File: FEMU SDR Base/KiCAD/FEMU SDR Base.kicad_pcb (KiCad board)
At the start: 4 copper layers, 164.8 x 164.8 mm, 33 parts, among them P2 SDR_Shield_1, P3 SDR_Shield_2, P8 Raspi_Power_Shield, U1 TPS562209, U2 SDR_1_LDO_1_2V, U3 SDR_2_LDO_1_2V, U4 SDR_1_LDO_3_3V, U5 SDR_2_LDO_3_3V

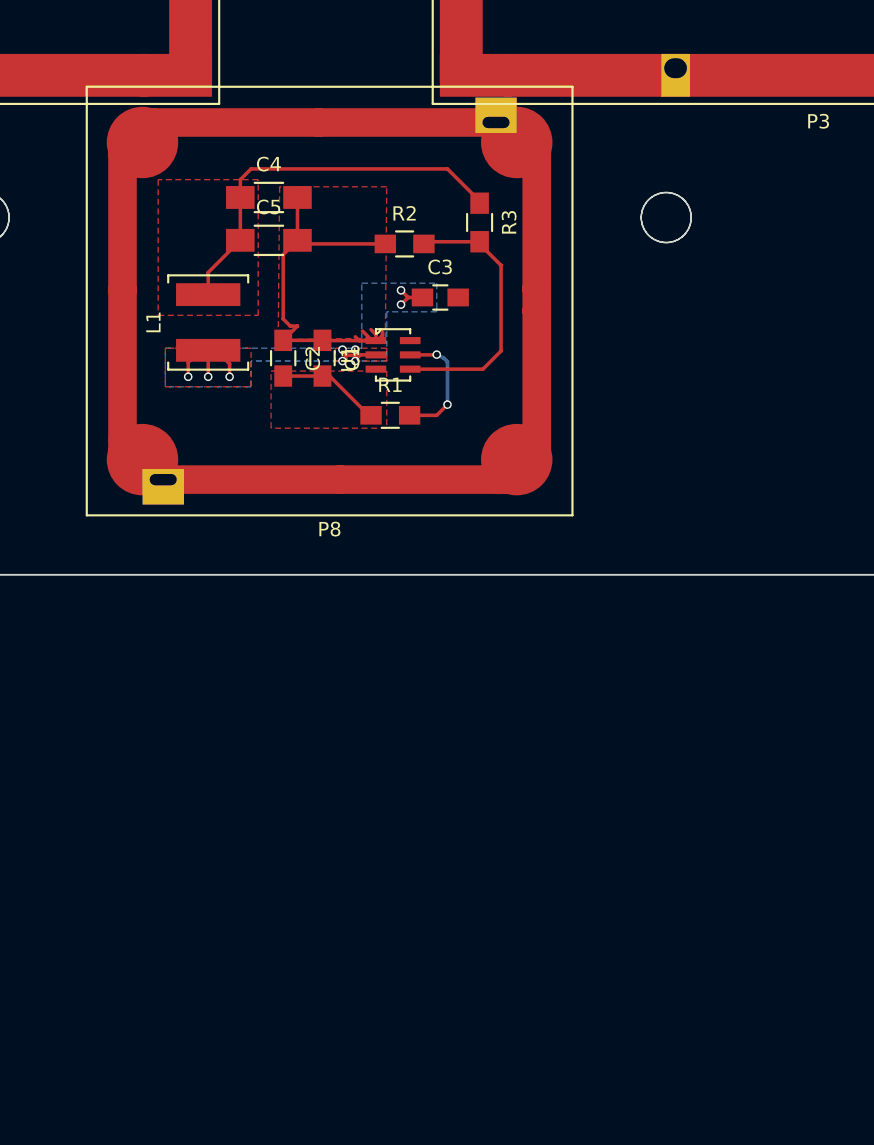
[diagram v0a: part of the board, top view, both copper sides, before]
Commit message: Added keepout zones for mechanical structures
Signed-off-by: hardiepienaar <hardiepienaar@gmail.com>
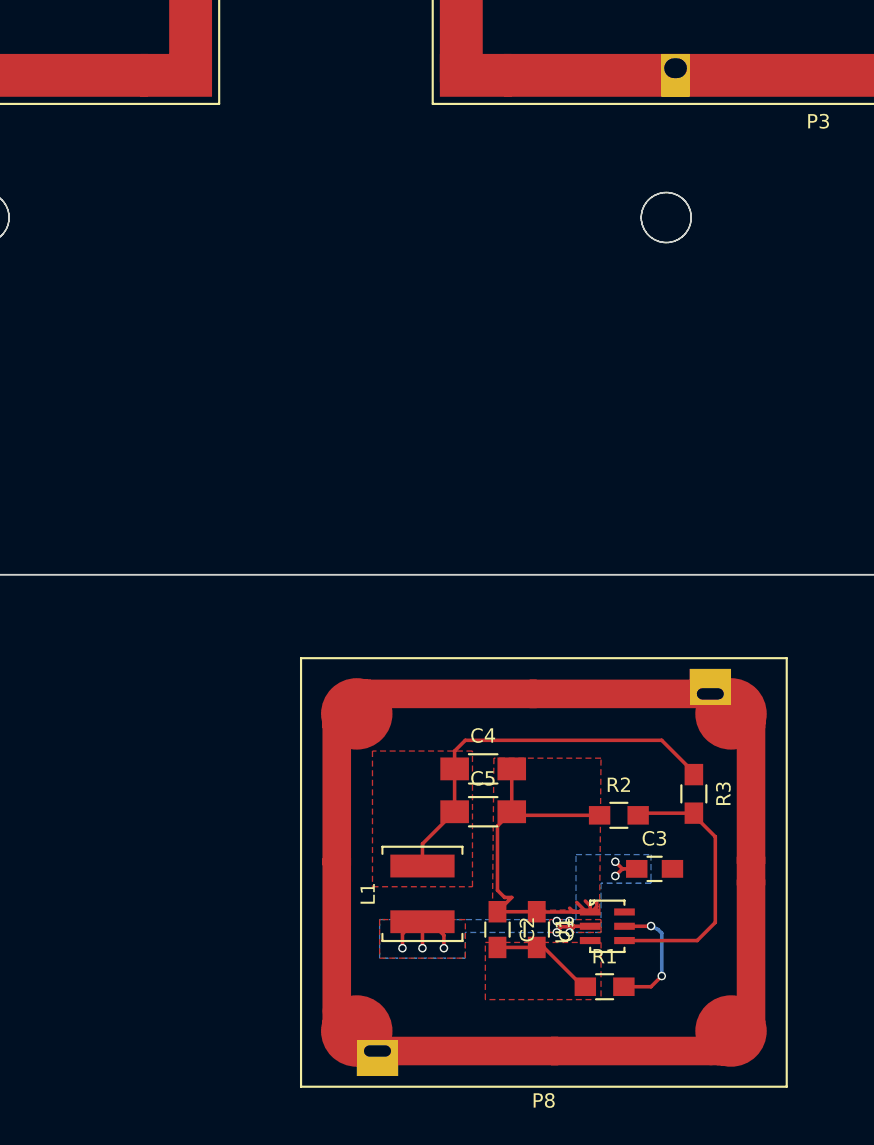
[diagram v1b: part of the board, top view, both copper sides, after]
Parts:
- moved C1 42.7 mm to (99.3, 181.9)
- moved C2 42.7 mm to (96.6, 181.9)
- moved C3 42.7 mm to (107.6, 177.7)
- moved C4 42.7 mm to (95.6, 170.7)
- moved C5 42.7 mm to (95.6, 173.7)
- moved L1 42.7 mm to (91.3, 179.4)
- moved P8 42.7 mm to (99.8, 177.9)
- moved R1 42.7 mm to (104.1, 185.9)
- moved R2 42.7 mm to (105.1, 173.9)
- moved R3 42.7 mm to (110.3, 172.4)
- moved U1 42.7 mm to (104.3, 181.7)
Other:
- board text added: "Cable tray area"
- board text added: "Power"

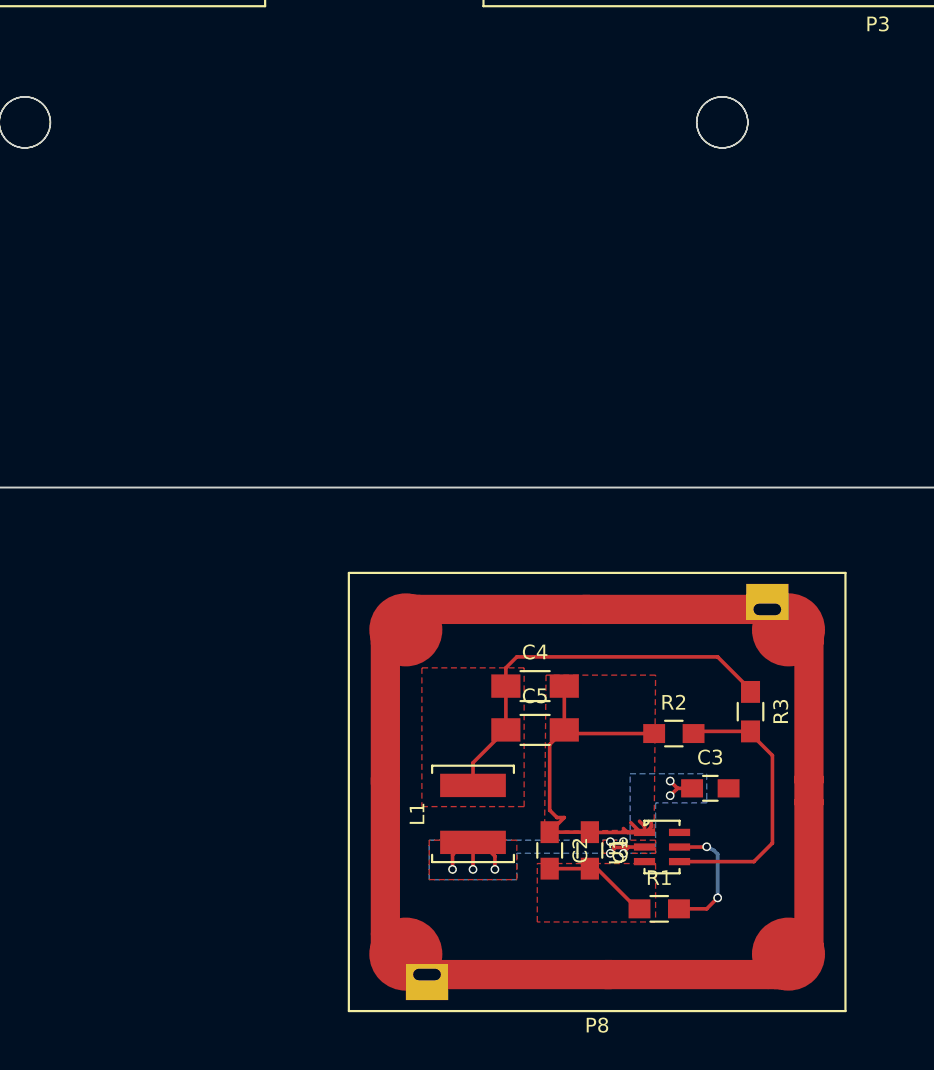
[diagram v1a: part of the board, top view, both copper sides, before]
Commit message: STATUS = FREE, RASPI PSU smaller layout, footprints swapped
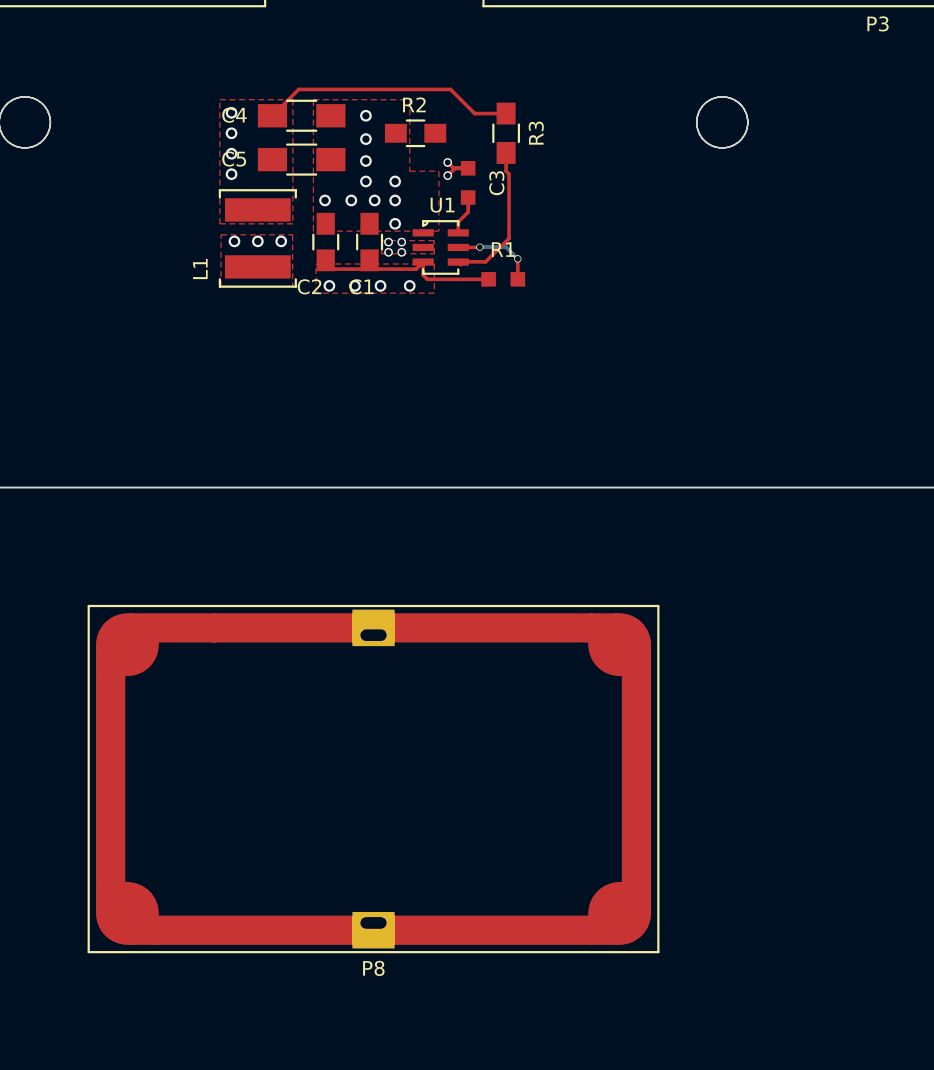
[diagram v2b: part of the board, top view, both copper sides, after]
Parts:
- P8: footprint ARB_foots:PCB_Shield_29x25mm -> ARB_foots:PCB_Shield_35x20mm
- moved R2 44.7 mm to (87.4, 132.8)
- moved C3 44.6 mm to (91.0, 136.2), turned to 270 degrees
- moved R1 44.4 mm to (93.4, 142.8)
- moved C2 44.4 mm to (81.2, 140.2)
- moved C1 44.3 mm to (84.2, 140.2)
- moved U1 43.8 mm to (89.1, 140.6)
- moved R3 43.0 mm to (93.6, 132.8)
- moved C4 42.2 mm to (79.6, 131.6)
- moved C5 42.2 mm to (79.6, 134.6)
- moved L1 42.1 mm to (76.6, 140.0)
- moved P8 15.3 mm to (84.5, 177.0)
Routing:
- net Earth: track 28.9 -> 0.39 mm
- net /VSW: track 14.4 -> 3.17 mm, vias 9 -> 2
- net GND: track 10.7 -> 0.00 mm
- net +5V: track 27.1 -> 17.4 mm
- net Net-(R2-Pad2): track 19.1 -> 10.3 mm
- net +12V: track 7.29 -> 12.7 mm
- net Net-(R1-Pad2): track 8.73 -> 5.82 mm
- net Net-(C3-Pad2): track 0.00 -> 2.70 mm
- net (no net): vias 0 -> 25
- added copper zone on 12V, net /VSW
- removed copper zone on B.Cu, net /VSW
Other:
- net class Default: via_dia 0.6 -> 0.5
- rule trace_min: 0.2 -> 0.155
- rule via_min_drill: 0.3 -> 0.33
- rule via_min_size: 0.4 -> 0.18

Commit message: Added pads for power, usb and pwm distribution
Signed-off-by: hardiepienaar <hardiepienaar@gmail.com>
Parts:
- added P10: PWM2, SMD_Packages:SMD-1206_Pol, F.Cu at (77.5, 28.2)
- added P11: PWM3, SMD_Packages:SMD-1206_Pol, F.Cu at (82.2, 28.2)
- added P12: PWM4, SMD_Packages:SMD-1206_Pol, F.Cu at (87.0, 28.2)
- added P13: PWM1, SMD_Packages:SMD-1206_Pol, F.Cu at (29.5, 127.8)
- added P14: PWM2, SMD_Packages:SMD-1206_Pol, F.Cu at (24.5, 41.8)
- added P15: PWM3, SMD_Packages:SMD-1206_Pol, F.Cu at (28.5, 41.8)
- added P16: PWM4, SMD_Packages:SMD-1206_Pol, F.Cu at (144.5, 41.8)
- added P17: 12V, SMD_Packages:1Pin, F.Cu at (128.5, 41.8)
- added P18: GND, SMD_Packages:1Pin, F.Cu at (134.5, 41.8)
- added P19: 12V, SMD_Packages:1Pin, F.Cu at (128.5, 127.8)
- added P20: GND, SMD_Packages:1Pin, F.Cu at (134.5, 127.8)
- added P21: S0GND, SMD_Packages:1Pin, F.Cu at (46.5, 177.8)
- added P22: S1GND, SMD_Packages:1Pin, F.Cu at (40.5, 177.8)
- added P23: S0DN, SMD_Packages:1Pin, F.Cu at (37.5, 186.2)
- added P24: S1DN, SMD_Packages:1Pin, F.Cu at (35.0, 185.8)
- added P25: S0DP, SMD_Packages:1Pin, F.Cu at (36.0, 186.8)
- added P26: S1DP, SMD_Packages:1Pin, F.Cu at (27.5, 185.8)
- added P27: PWM0, SMD_Packages:SMD-1206_Pol, F.Cu at (68.0, 28.2)
- added P28: PWM5, SMD_Packages:SMD-1206_Pol, F.Cu at (91.8, 28.2)
- added P29: PWM6, SMD_Packages:SMD-1206_Pol, F.Cu at (96.5, 28.2)
- added P30: PWM7, SMD_Packages:SMD-1206_Pol, F.Cu at (101.2, 28.2)
- added P31: PWM0, SMD_Packages:SMD-1206_Pol, F.Cu at (24.5, 127.8)
- added P32: PWM5, SMD_Packages:SMD-1206_Pol, F.Cu at (140.5, 41.8)
- added P33: PWM6, SMD_Packages:SMD-1206_Pol, F.Cu at (144.5, 127.8)
- added P34: PWM7, SMD_Packages:SMD-1206_Pol, F.Cu at (140.5, 127.8)
- added P4: 12V, SMD_Packages:1Pin, F.Cu at (40.5, 41.8)
- added P5: GND, SMD_Packages:1Pin, F.Cu at (36.0, 127.8)
- added P6: 12V, SMD_Packages:1Pin, F.Cu at (41.5, 127.8)
- added P7: GND, SMD_Packages:1Pin, F.Cu at (34.5, 41.8)
- added P9: PWM1, SMD_Packages:SMD-1206_Pol, F.Cu at (72.8, 28.2)
- moved P8 42.0 mm to (84.5, 135.0)
- moved C1 2.00 mm to (84.2, 138.2)
- moved C2 2.00 mm to (81.2, 138.2)
- moved C3 2.00 mm to (91.0, 134.2)
- moved C4 2.00 mm to (79.6, 129.6)
- moved C5 2.00 mm to (79.6, 132.6)
- moved L1 2.00 mm to (76.6, 138.0)
- moved R1 2.00 mm to (93.4, 140.8)
- moved R2 2.00 mm to (87.4, 130.8)
- moved R3 2.00 mm to (93.6, 130.8)
- moved U1 2.00 mm to (89.1, 138.6)
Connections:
- C1 pad 1: Earth -> GND
- C2 pad 1: Earth -> GND
- C4 pad 2: Earth -> GND
- C5 pad 2: Earth -> GND
- R2 pad 1: Earth -> GND
- U1 pad 1: Earth -> GND
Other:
- board size 164.8 x 164.8 mm -> 164.8 x 186.6 mm

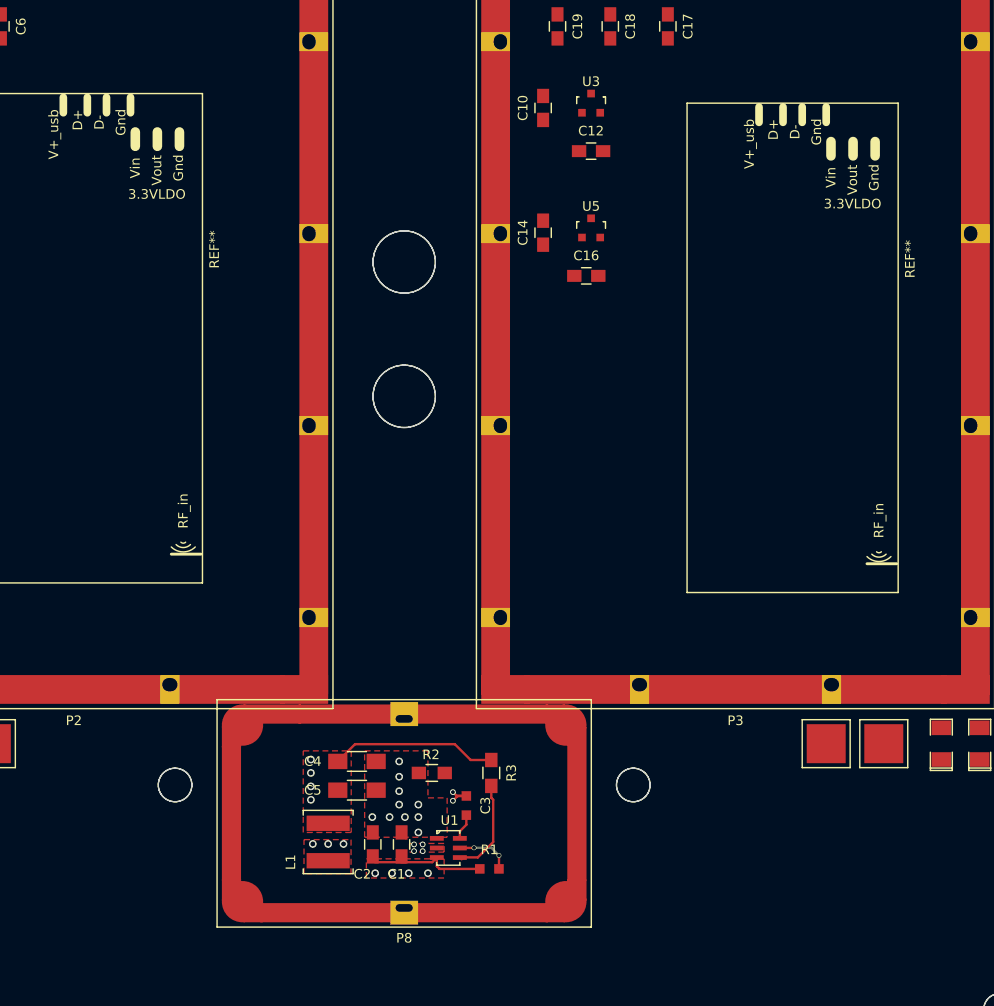
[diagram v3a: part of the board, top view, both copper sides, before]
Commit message: STATUS=FREE, RasPi Power fit in
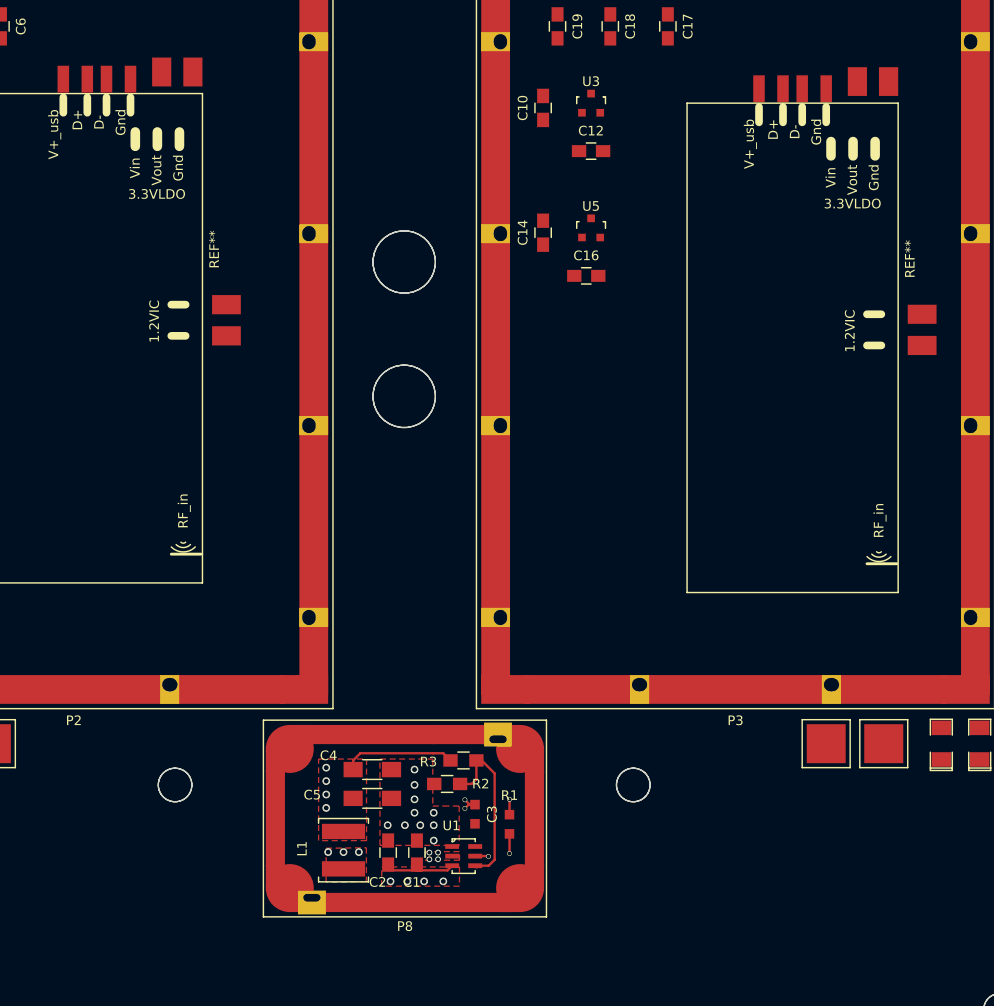
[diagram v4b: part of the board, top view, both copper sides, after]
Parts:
- P8: footprint ARB_foots:PCB_Shield_35x20mm -> ARB_foots:PCB_Shield_26x16mm
- moved R1 5.10 mm to (95.5, 136.2), turned to 270 degrees
- moved R3 3.18 mm to (90.7, 129.5), turned to 0 degrees
- moved R2 1.97 mm to (89.0, 131.9)
- moved C4 1.81 mm to (81.2, 130.4)
- moved C5 1.81 mm to (81.2, 133.4)
- moved L1 1.81 mm to (78.2, 138.8)
- moved C1 1.81 mm to (85.8, 139.1)
- moved C2 1.81 mm to (82.8, 139.1)
- moved U1 1.81 mm to (90.7, 139.5)
- moved C3 1.27 mm to (91.9, 135.1)
- moved P8 0.54 mm to (84.6, 135.6)
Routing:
- net Net-(R2-Pad2): track 10.3 -> 17.9 mm
- net +5V: track 17.4 -> 11.7 mm
- net +12V: track 12.7 -> 8.79 mm, vias 0 -> 1
- net Net-(C3-Pad2): track 2.70 -> 0.00 mm
- net /VSW: track 3.17 -> 2.47 mm
